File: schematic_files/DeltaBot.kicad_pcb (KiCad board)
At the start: 2 copper layers, 241.5 x 110.5 mm, 15 parts, among them J1 USB C PD Modulle, J2 LIDAR, J3 MOTOR_L, J4 MOTOR_R, SW1 SW_SPDT, U1 RPLIDAR C1, U1 Radxa_ROCK5B, U2 Buck Converter

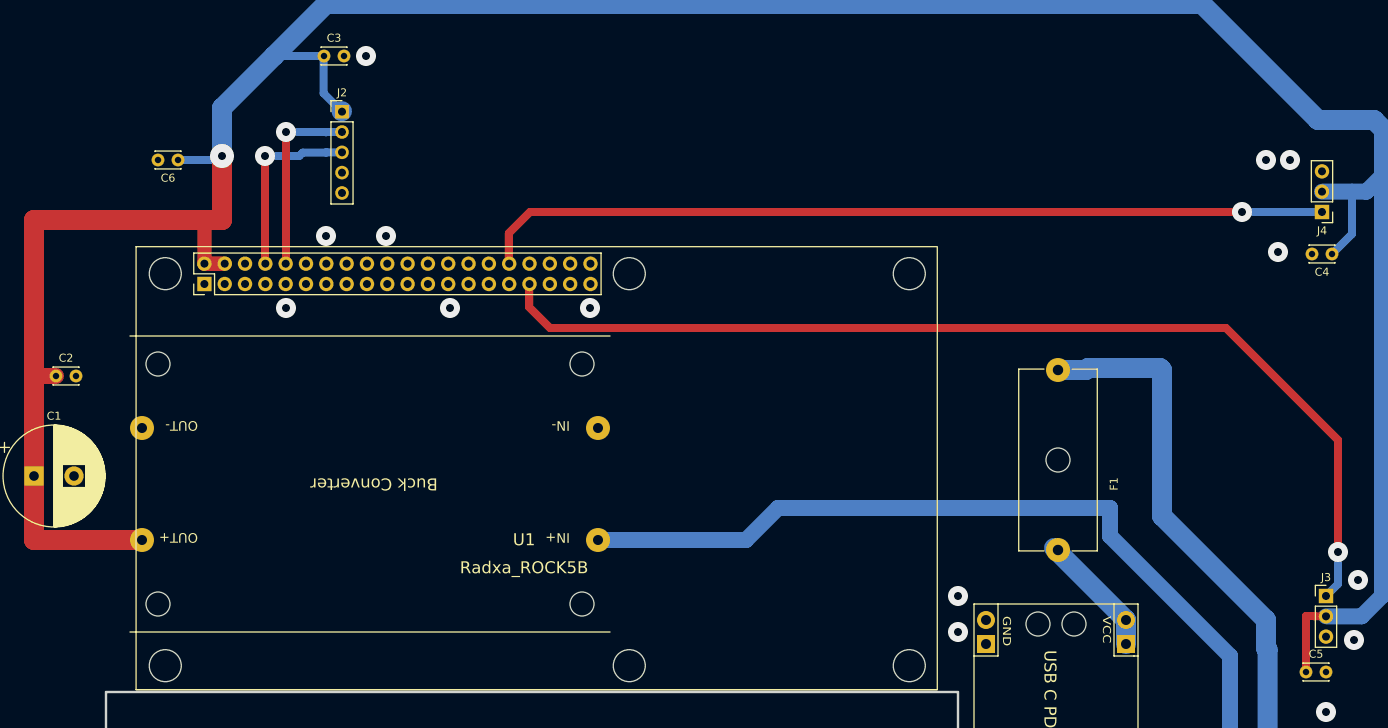
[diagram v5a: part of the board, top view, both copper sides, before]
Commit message: Updated the PCB according to Andrew's feedback.
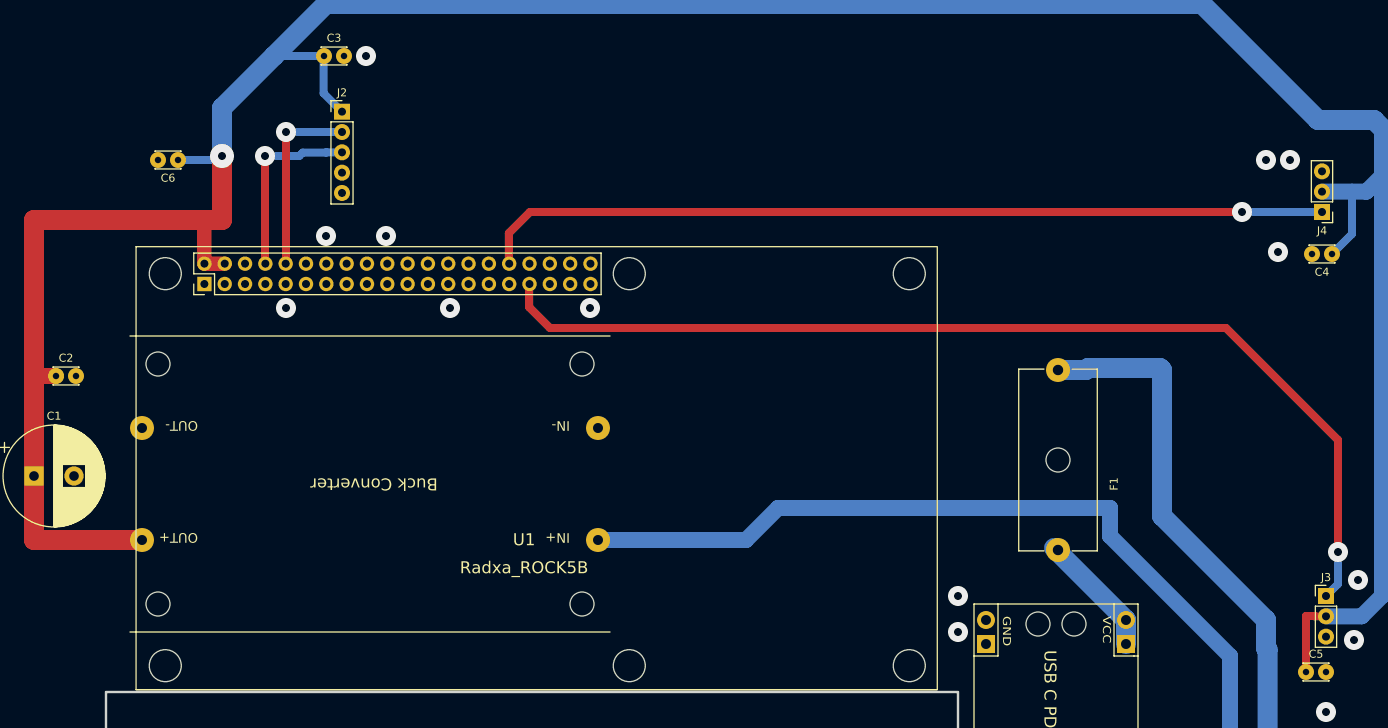
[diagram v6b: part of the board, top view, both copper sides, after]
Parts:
- J2: footprint Connector_PinHeader_2.54mm:PinHeader_1x05_P2.54mm_Vertical -> deltabot:PinHeader_1x05_P2.54mm_Vertical
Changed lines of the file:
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@@
 		(pcbplotparams
 			(layerselection 0x00000000_00000000_55555555_55555555)
-			(plot_on_all_layers_selection 0x00000000_00000000_00000002_020a00aa)
+			(plot_on_all_layers_selection 0x00000000_00000000_00000002_020000aa)
 			(disableapertmacros no)
-			(usegerberextensions no)
+			(usegerberextensions yes)
 			(usegerberattributes yes)
 			(usegerberadvancedattributes yes)
@@
 			(crossoutdnponfab yes)
 			(subtractmaskfromsilk no)
-			(outputformat 4)
+			(outputformat 1)
 			(mirror no)
 			(drillshape 0)
 			(scaleselection 1)
-			(outputdirectory "/tmp/drill")
+			(outputdirectory "/tmp/gerber/")
 		)
 	)
@@
 		(pad "1" thru_hole circle
 			(at 0 0 180)
-			(size 1.6 1.6)
+			(size 2 2)
 			(drill 0.8)
 			(layers "*.Cu" "*.Mask")
@@
 		(pad "2" thru_hole circle
 			(at 2.5 0 180)
-			(size 1.6 1.6)
+			(size 2 2)
 			(drill 0.8)
 			(layers "*.Cu" "*.Mask")
@@
 		(pad "1" thru_hole rect
 			(at 0 0)
-			(size 1.8 1.8)
+			(size 2 2)
 			(drill 1)
 			(layers "*.Cu" "*.Mask")
@@
 		(pad "2" thru_hole oval
 			(at 0 2.54)
-			(size 1.8 1.8)
+			(size 2 2)
 			(drill 1)
 			(layers "*.Cu" "*.Mask")
@@
 		(pad "3" thru_hole oval
 			(at 0 5.08)
-			(size 1.8 1.8)
+			(size 2 2)
 			(drill 1)
 			(layers "*.Cu" "*.Mask")
@@
 		(embedded_fonts no)
 	)
-	(footprint "Connector_PinHeader_2.54mm:PinHeader_1x05_P2.54mm_Vertical"
+	(footprint "deltabot:PinHeader_1x05_P2.54mm_Vertical"
 		(layer "F.Cu")
 		(at 79 53.96)
@@
 			)
 		)
-		(property "Datasheet" "~"
+		(property "Datasheet" ""
 			(at 0 0 0)
 			(layer "F.Fab")
@@
 			)
 		)
-		(property "Description" "Generic connector, single row, 01x05, script generated (kicad-library-utils/schlib/autogen/connector/)"
+		(property "Description" ""
 			(at 0 0 0)
 			(layer "F.Fab")
@@
 		(pad "1" thru_hole rect
 			(at 0 0)
-			(size 1.7 1.7)
+			(size 2 2)
 			(drill 1)
 			(layers "*.Cu" "*.Mask")
@@
 		(pad "2" thru_hole circle
 			(at 0 2.54)
-			(size 1.7 1.7)
+			(size 2 2)
 			(drill 1)
 			(layers "*.Cu" "*.Mask")
@@
 		(pad "3" thru_hole circle
 			(at 0 5.08)
-			(size 1.7 1.7)
+			(size 2 2)
 			(drill 1)
 			(layers "*.Cu" "*.Mask")
@@
 		(pad "4" thru_hole circle
 			(at 0 7.62)
-			(size 1.7 1.7)
+			(size 2 2)
 			(drill 1)
 			(layers "*.Cu" "*.Mask")
@@
 		(pad "5" thru_hole circle
 			(at 0 10.16)
-			(size 1.7 1.7)
+			(size 2 2)
 			(drill 1)
 			(layers "*.Cu" "*.Mask")
@@
 		(pad "1" thru_hole circle
 			(at 0 0)
-			(size 1.6 1.6)
+			(size 2 2)
 			(drill 0.8)
 			(layers "*.Cu" "*.Mask")
@@
 		(pad "2" thru_hole circle
 			(at 2.5 0)
-			(size 1.6 1.6)
+			(size 2 2)
 			(drill 0.8)
 			(layers "*.Cu" "*.Mask")
@@
 		(pad "1" thru_hole rect
 			(at 0 0 180)
-			(size 1.8 1.8)
+			(size 2 2)
 			(drill 1)
 			(layers "*.Cu" "*.Mask")
@@
 		(pad "2" thru_hole oval
 			(at 0 2.54 180)
-			(size 1.8 1.8)
+			(size 2 2)
 			(drill 1)
 			(layers "*.Cu" "*.Mask")
@@
 		(pad "3" thru_hole oval
 			(at 0 5.08 180)
-			(size 1.8 1.8)
+			(size 2 2)
 			(drill 1)
 			(layers "*.Cu" "*.Mask")
@@
 		(pad "1" thru_hole circle
 			(at 0 0)
-			(size 1.6 1.6)
+			(size 2 2)
 			(drill 0.8)
 			(layers "*.Cu" "*.Mask")
@@
 		(pad "2" thru_hole circle
 			(at 2.5 0)
-			(size 1.6 1.6)
+			(size 2 2)
 			(drill 0.8)
 			(layers "*.Cu" "*.Mask")
@@
 		(pad "1" thru_hole circle
 			(at 0 0)
-			(size 1.6 1.6)
+			(size 2 2)
 			(drill 0.8)
 			(layers "*.Cu" "*.Mask")
@@
 		(pad "2" thru_hole circle
 			(at 2.5 0)
-			(size 1.6 1.6)
+			(size 2 2)
 			(drill 0.8)
 			(layers "*.Cu" "*.Mask")
@@
 		(pad "1" thru_hole circle
 			(at 0 0 180)
-			(size 1.6 1.6)
+			(size 2 2)
 			(drill 0.8)
 			(layers "*.Cu" "*.Mask")
@@
 		(pad "2" thru_hole circle
 			(at 2.5 0 180)
-			(size 1.6 1.6)
+			(size 2 2)
 			(drill 0.8)
 			(layers "*.Cu" "*.Mask")
@@
 	)
 	(segment
-		(start 77.04 56.5)
-		(end 79 56.5)
-		(width 1)
-		(layer "B.Cu")
-		(net 10)
-	)
-	(segment
-		(start 76.96 56.5)
-		(end 77 56.54)
-		(width 1)
-		(layer "B.Cu")
-		(net 10)
-	)
-	(segment
 		(start 72 56.5)
-		(end 76.96 56.5)
-		(width 1)
-		(layer "B.Cu")
-		(net 10)
-	)
-	(segment
-		(start 77 56.54)
-		(end 77.04 56.5)
+		(end 79 56.5)
 		(width 1)
 		(layer "B.Cu")
@@
 		(width 2.5)
 		(layer "B.Cu")
-		(net 26)
-	)
-	(segment
-		(start 78.94 53.9)
-		(end 79 53.9)
-		(width 2.5)
-		(layer "B.Cu")
